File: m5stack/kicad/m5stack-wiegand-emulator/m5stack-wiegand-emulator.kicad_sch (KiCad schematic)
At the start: 51 parts, among them J1 2x15 socket header, J2 2x15 pin header, J3 1x5 female, T1 TestPoint, T2 TestPoint, T3 TestPoint, T4 TestPoint, U1 RP2040, U2 ISOW7841, U3 SN74LVC2G126-EP, U5 SN74AHCT1G125, U6 FISM 1769405241

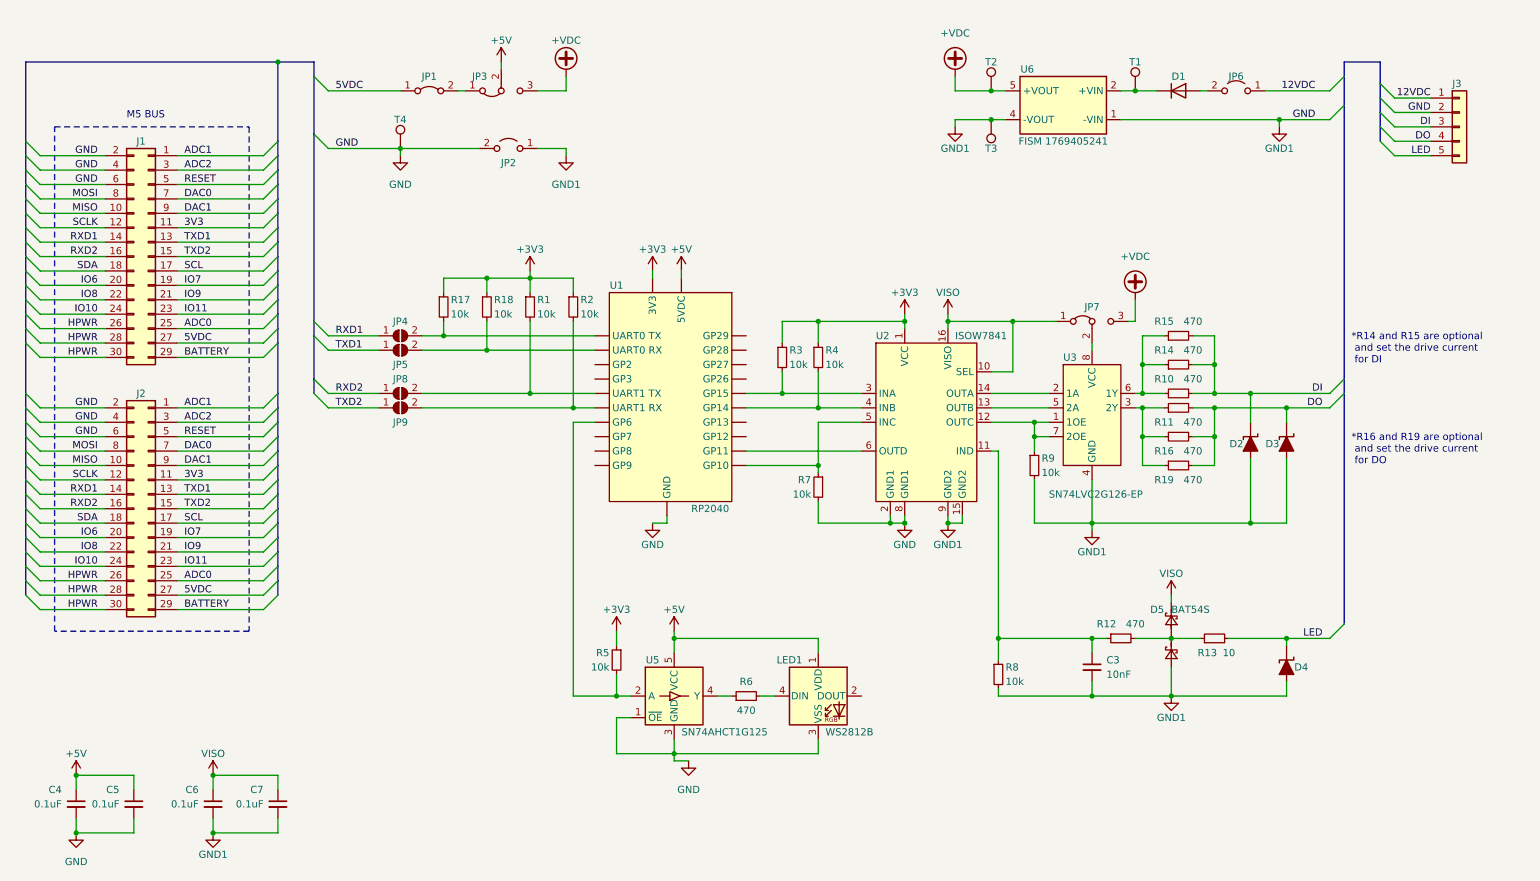
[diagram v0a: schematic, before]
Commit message: M5: replaced WS2812 driver with output from ISOW7843
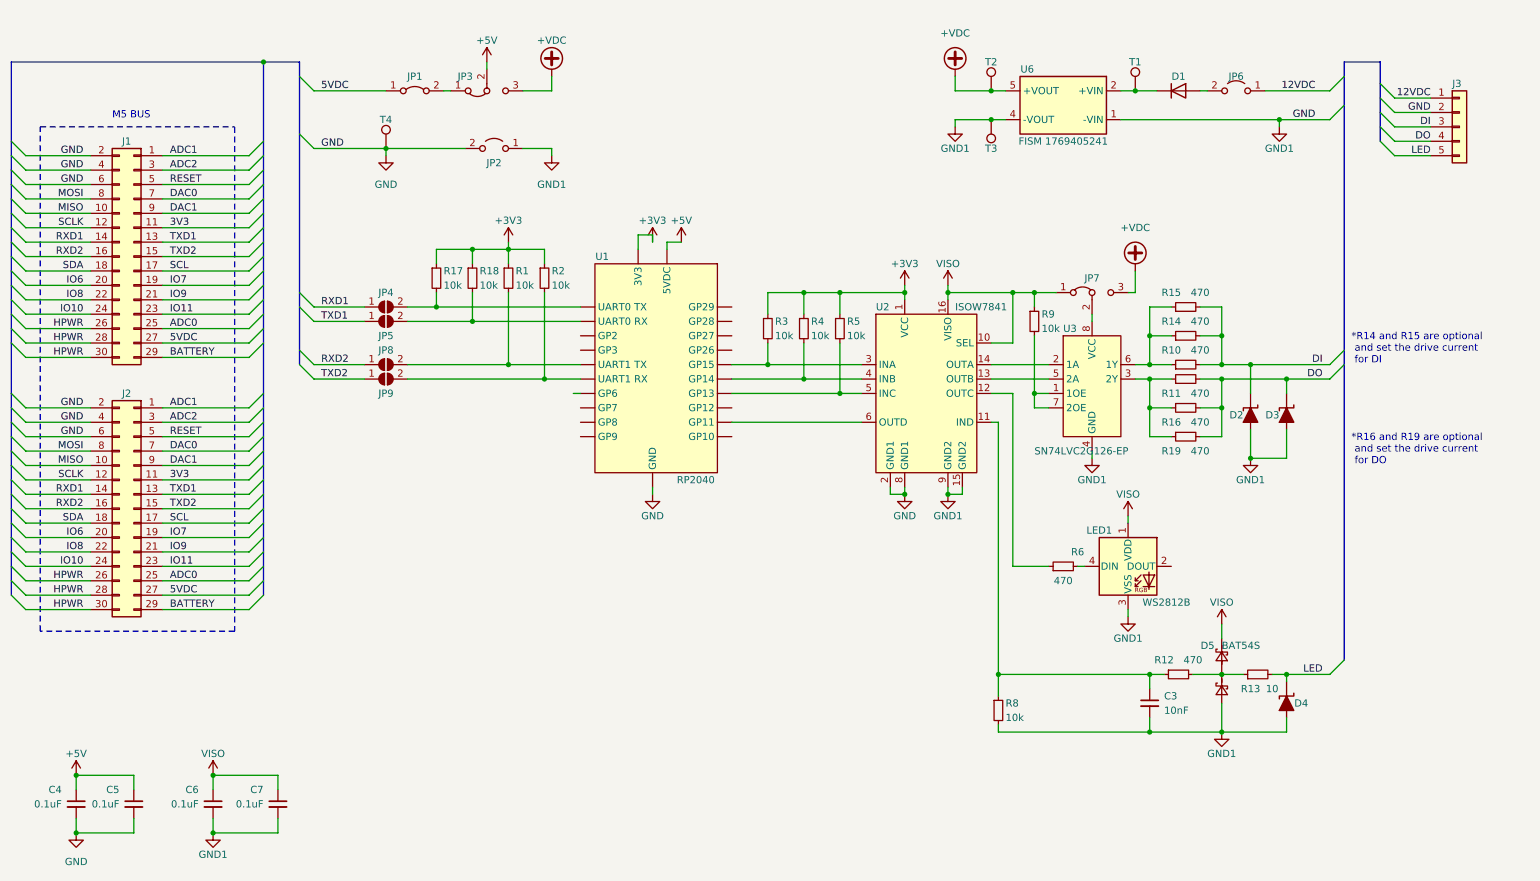
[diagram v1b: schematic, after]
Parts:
- removed R7: 10k, Resistor_SMD:R_0805_2012Metric_Pad1.20x1.40mm_HandSolder, symbol Device:R_Small
- removed U5: SN74AHCT1G125, Package_TO_SOT_SMD:SOT-23-5, symbol uhppoted:SN74AHCT1G125
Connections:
- net +5V: no longer LED1.1 (VDD)
- net GND: no longer R9.2
- net VISO: now also LED1.1 (VDD), R9.1
- net at U3.1 (1OE), U3.7 (2OE): now also R9.2; no longer R9.1, U2.12 (OUTC)
- net at U2.5 (INC): now also R5.2, U1.10 (GP13); no longer U1.13 (GP10)
- net at U1.17 (GP6): no longer R5.2
- net at R6.1: now also U2.12 (OUTC)
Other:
- moved on the sheet: C3, D2, D3, D4, D5, J1, J2, JP1, JP2, JP3, JP4, JP5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

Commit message: M5: replaced THT TranzOrbs with SMD
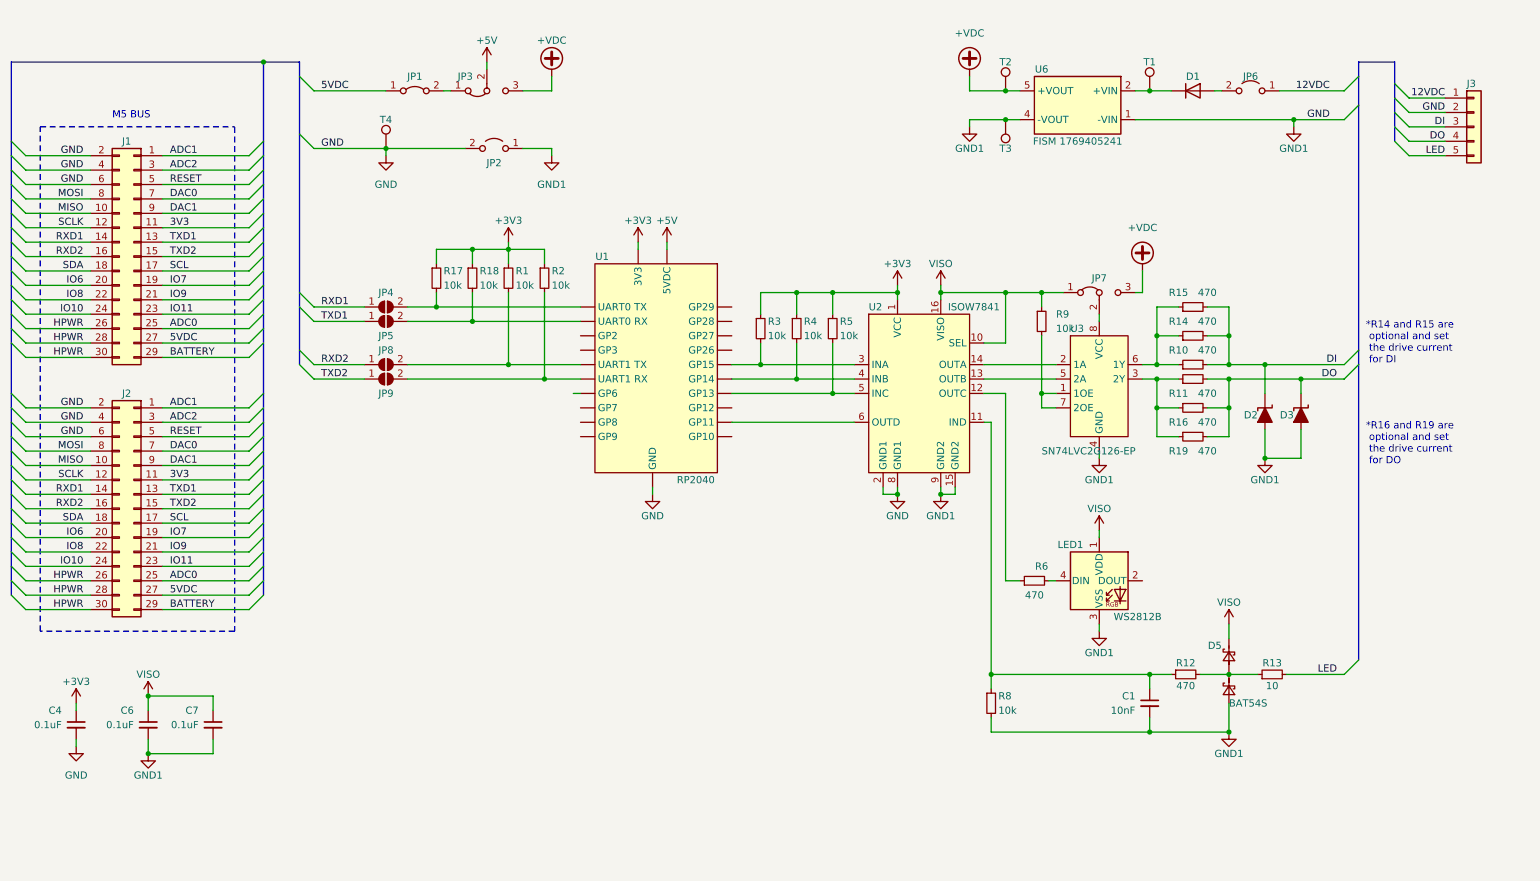
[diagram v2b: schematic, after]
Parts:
- removed C5: 0.1uF, Capacitor_SMD:C_0805_2012Metric_Pad1.18x1.45mm_HandSolder, symbol Device:C_Small
- removed D4: SA5.0A, Diode_THT:D_DO-15_P2.54mm_Vertical_KathodeUp, symbol uhppoted:TVS_Unidirectional
- D2, D3: value SA5.0A -> MSP5.0A; footprint Diode_THT:D_DO-15_P2.54mm_Vertical_KathodeUp -> Diode_SMD:D_MicroSMP_AK
- renumbered C3 to C1
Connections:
- net +3V3: now also C4.1
- net +5V: no longer C4.1
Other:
- moved on the sheet: C4, C6, C7, D1, D2, D3, D5, J3, JP6, JP7, LED1, R10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

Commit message: M5: reworked PCB footprints for overlap
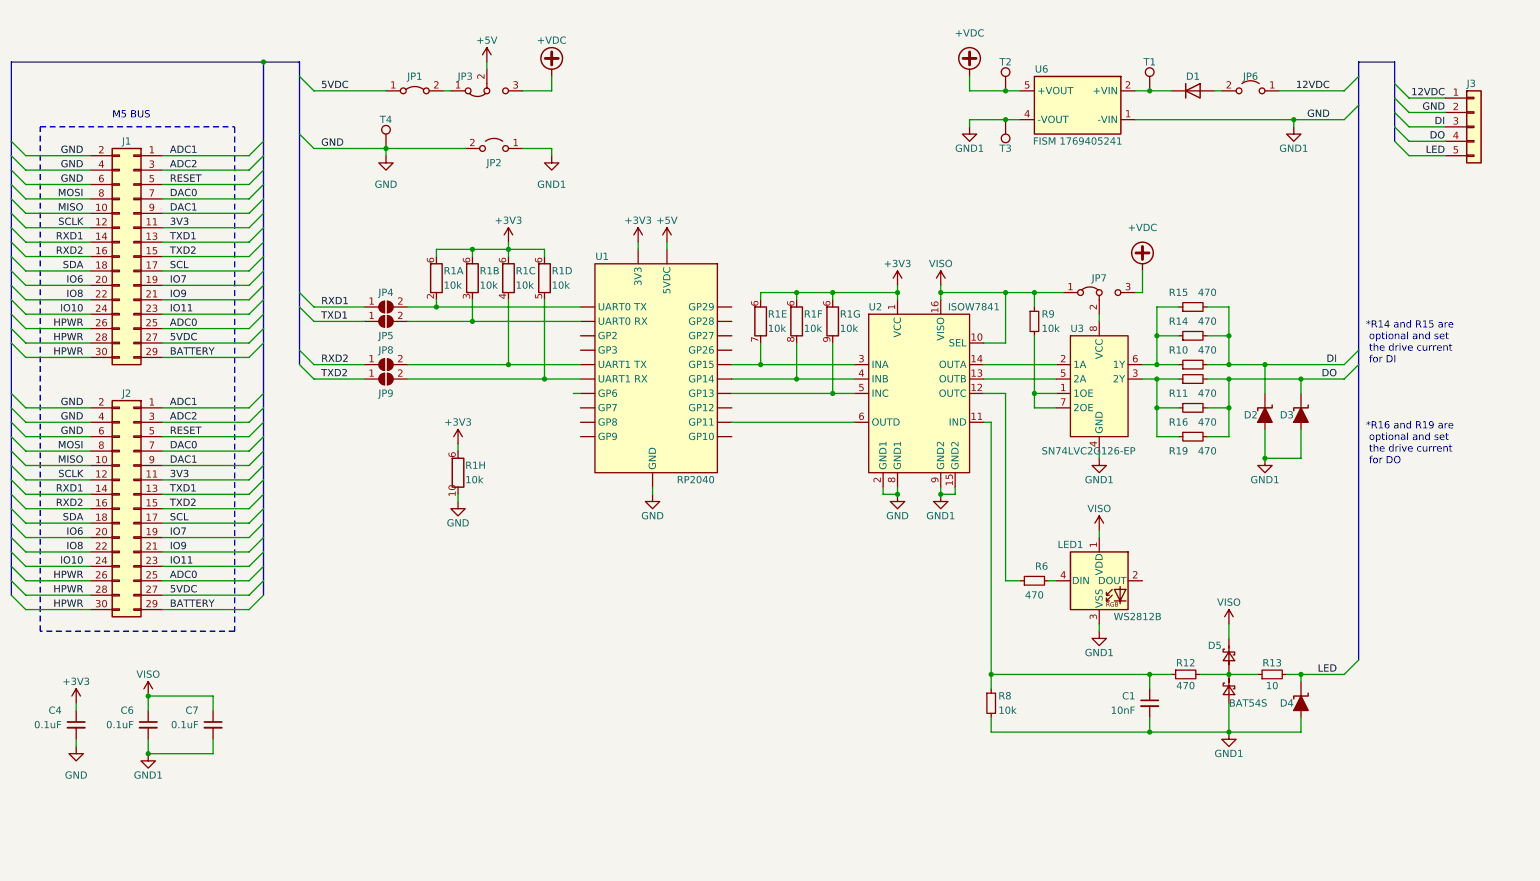
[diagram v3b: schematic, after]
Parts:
- removed R1, R18, R2, R3, R4, R5: 10k, Resistor_SMD:R_0805_2012Metric_Pad1.20x1.40mm_HandSolder, symbol Device:R_Small
- added D4: MSP5.0A, Diode_SMD:D_MicroSMP_AK, symbol uhppoted:TVS_Unidirectional
- added unit 6 of R1
- added unit 7 of R1
- added unit 8 of R1
- added unit 3 of R1
- added unit 5 of R1
- added unit 2 of R1
- added unit 4 of R1
- J3: footprint Connector_Molex:Molex_Micro-Latch_53254-0570_1x05_P2.00mm_Horizontal -> Connector_Molex:Molex_PicoBlade_53261-0571_1x05-1MP_P1.25mm_Horizontal; symbol Connector_Generic:Conn_01x05 -> uhppoted:Molex_PicoBlade_1x05
- R1: renamed from R17; footprint Resistor_SMD:R_0805_2012Metric_Pad1.20x1.40mm_HandSolder -> uhppoted:RESCAV63P320X160X65-10N; symbol Device:R_Small -> uhppoted:EXB-D10C103J_Split
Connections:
- net +3V3: now also R1.6 (R1), R1.6 (R1), R1.6 (R1), R1.6 (R1), R1.6 (R1), R1.6 (R1), R1.6 (R1), R1.6 (R1); no longer R1.1
- net GND: now also D4.2 (A2), R1.10 (R8.2)
- net LED: now also D4.1 (A1)
- net at JP5.2 (B), U1.22 (GP1): now also R1.3 (R2.2)
- net at U1.9 (GP14), U2.4 (INB): now also R1.8 (R6.2)
- net at U1.10 (GP13), U2.5 (INC): now also R1.9 (R7.2)
- net at U1.8 (GP15), U2.3 (INA): now also R1.7 (R5.2)
- net at JP9.2 (B), U1.18 (GP5): now also R1.5 (R4.2)
- net at JP8.2 (B), U1.19 (GP4): now also R1.4 (R3.2)
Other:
- moved on the sheet: R9

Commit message: M5: added fiducial marks and logo/revision
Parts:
- D2, D3, D4: footprint Diode_SMD:D_MicroSMP_AK -> uhppoted:MSP5.0A
- R1: footprint uhppoted:RESCAV63P320X160X65-10N -> uhppoted:EXB-D10C103J
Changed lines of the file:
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@@
       (effects (font (size 1.27 1.27)) (justify left))
     )
-    (property "Footprint" "uhppoted:RESCAV63P320X160X65-10N" (at 154.94 92.71 0)
+    (property "Footprint" "uhppoted:EXB-D10C103J" (at 154.94 92.71 0)
       (effects (font (size 1.27 1.27)) hide)
     )
@@
       (effects (font (size 1.27 1.27)) (justify left))
     )
-    (property "Footprint" "uhppoted:RESCAV63P320X160X65-10N" (at 161.29 92.71 0)
+    (property "Footprint" "uhppoted:EXB-D10C103J" (at 161.29 92.71 0)
       (effects (font (size 1.27 1.27)) hide)
     )
@@
       (effects (font (size 1.27 1.27)) (justify left))
     )
-    (property "Footprint" "uhppoted:RESCAV63P320X160X65-10N" (at 95.25 119.38 0)
+    (property "Footprint" "uhppoted:EXB-D10C103J" (at 95.25 119.38 0)
       (effects (font (size 1.27 1.27)) hide)
     )
@@
       (effects (font (size 1.27 1.27)) (justify left))
     )
-    (property "Footprint" "uhppoted:RESCAV63P320X160X65-10N" (at 104.14 85.09 0)
+    (property "Footprint" "uhppoted:EXB-D10C103J" (at 104.14 85.09 0)
       (effects (font (size 1.27 1.27)) hide)
     )
@@
       (effects (font (size 1.27 1.27)) (justify left))
     )
-    (property "Footprint" "uhppoted:RESCAV63P320X160X65-10N" (at 148.59 92.71 0)
+    (property "Footprint" "uhppoted:EXB-D10C103J" (at 148.59 92.71 0)
       (effects (font (size 1.27 1.27)) hide)
     )
@@
       (effects (font (size 1.27 1.27)) (justify left))
     )
-    (property "Footprint" "uhppoted:RESCAV63P320X160X65-10N" (at 91.44 85.09 0)
+    (property "Footprint" "uhppoted:EXB-D10C103J" (at 91.44 85.09 0)
       (effects (font (size 1.27 1.27)) hide)
     )
@@
       (effects (font (size 1.27 1.27)) (justify left) hide)
     )
-    (property "Footprint" "Diode_SMD:D_MicroSMP_AK" (at 246.38 142.24 0)
+    (property "Footprint" "uhppoted:MSP5.0A" (at 246.38 142.24 0)
       (effects (font (size 1.27 1.27)) hide)
     )
@@
       (effects (font (size 1.27 1.27)) (justify left))
     )
-    (property "Footprint" "uhppoted:RESCAV63P320X160X65-10N" (at 97.79 85.09 0)
+    (property "Footprint" "uhppoted:EXB-D10C103J" (at 97.79 85.09 0)
       (effects (font (size 1.27 1.27)) hide)
     )
@@
       (effects (font (size 1.27 1.27)) (justify left))
     )
-    (property "Footprint" "uhppoted:RESCAV63P320X160X65-10N" (at 110.49 85.09 0)
+    (property "Footprint" "uhppoted:EXB-D10C103J" (at 110.49 85.09 0)
       (effects (font (size 1.27 1.27)) hide)
     )
@@
       (effects (font (size 1.27 1.27)) (justify left) hide)
     )
-    (property "Footprint" "Diode_SMD:D_MicroSMP_AK" (at 240.03 91.44 0)
+    (property "Footprint" "uhppoted:MSP5.0A" (at 240.03 91.44 0)
       (effects (font (size 1.27 1.27)) hide)
     )
@@
       (effects (font (size 1.27 1.27)) (justify left) hide)
     )
-    (property "Footprint" "Diode_SMD:D_MicroSMP_AK" (at 246.38 91.44 0)
-      (effects (font (size 1.27 1.27)) hide)
-    )
+    (property "Footprint" "uhppoted:MSP5.0A" (at 246.38 91.44 0)
+      (effects (font (size 1.27 1.27)) hide)
+    )

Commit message: M5: routing PCB
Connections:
- net 12VDC: now also J3.5 (Pin_5), JP6.2 (B); no longer J3.1 (Pin_1), JP6.1 (A)
- net DO: now also J3.2 (Pin_2); no longer J3.4 (Pin_4)
- net GND: now also J3.4 (Pin_4); no longer J3.2 (Pin_2)
- net LED: now also J3.1 (Pin_1); no longer J3.5 (Pin_5)
- net at D1.2 (A): now also JP6.1 (A); no longer JP6.2 (B)
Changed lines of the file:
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@@
     )
   )
-  (symbol (lib_id "uhppoted:Molex_PicoBlade_1x05") (at 276.86 41.91 0) (unit 1)
+  (symbol (lib_id "uhppoted:Molex_PicoBlade_1x05") (at 276.86 41.91 0) (mirror x) (unit 1)
     (in_bom yes) (on_board yes) (dnp no)
     (property "Reference" "J3" (at 275.59 34.29 0)
       (effects (font (size 1.27 1.27)) (justify left))
     )
-    (property "Value" "1x5 female" (at 279.4 43.18 0)
+    (property "Value" "1x5 female" (at 279.4 40.64 0)
       (effects (font (size 1.27 1.27)) (justify left) hide)
     )
@@
     )
   )
-  (symbol (lib_id "Jumper:Jumper_2_Open") (at 237.49 35.56 0) (mirror y) (unit 1)
+  (symbol (lib_id "Jumper:Jumper_2_Open") (at 237.49 35.56 0) (unit 1)
     (in_bom yes) (on_board yes) (dnp no)
     (property "Reference" "JP6" (at 237.49 33.02 0)
